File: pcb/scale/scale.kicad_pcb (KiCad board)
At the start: 2 copper layers, 103.8 x 47.9 mm, 89 parts, among them J1 USB_C_Receptacle_USB2.0, J2 Conn_01x07, J3 Conn_01x04, SW1 SW_Push, SW10 SW_Push, SW11 SW_Push, SW12 SW_Push, SW13 SW_Push, SW14 SW_Push, SW15 SW_Push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

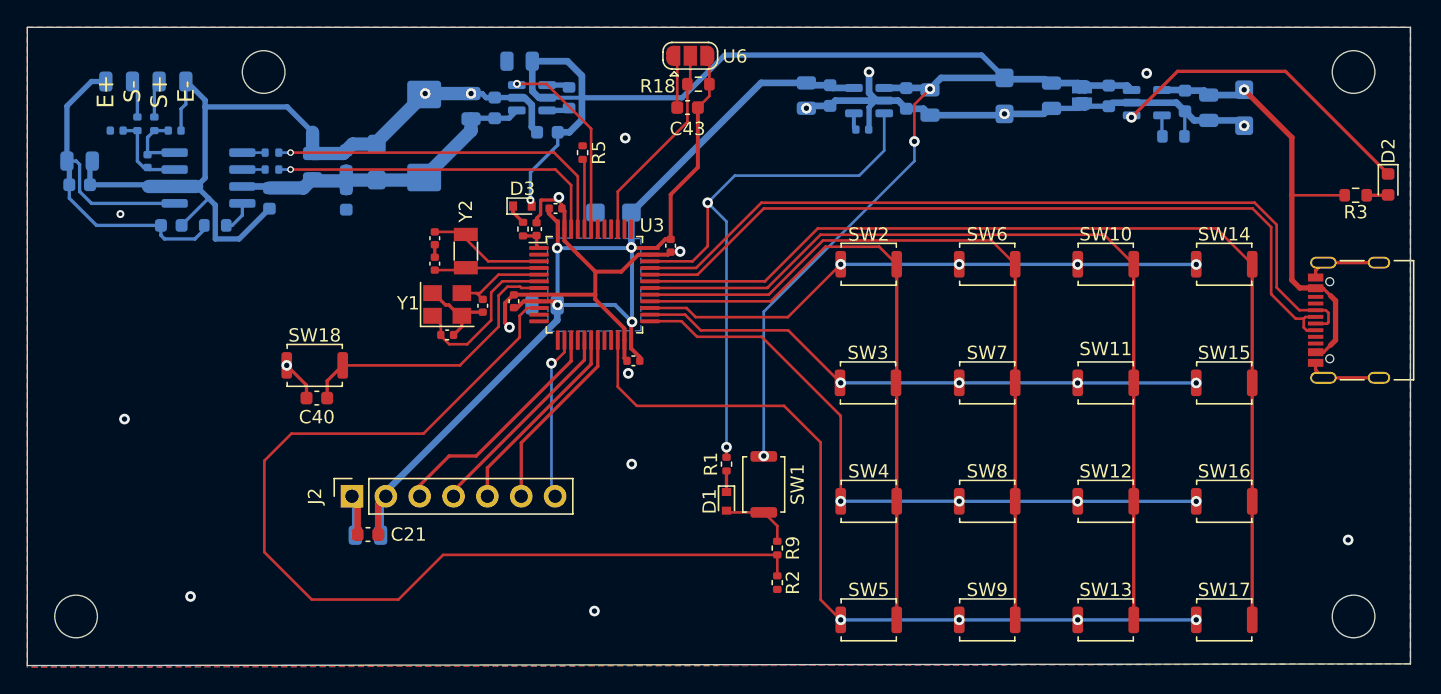
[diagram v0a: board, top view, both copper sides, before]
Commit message: 部分信号线加粗到0.25mm，电荷泵BATT+加粗到0.5mm
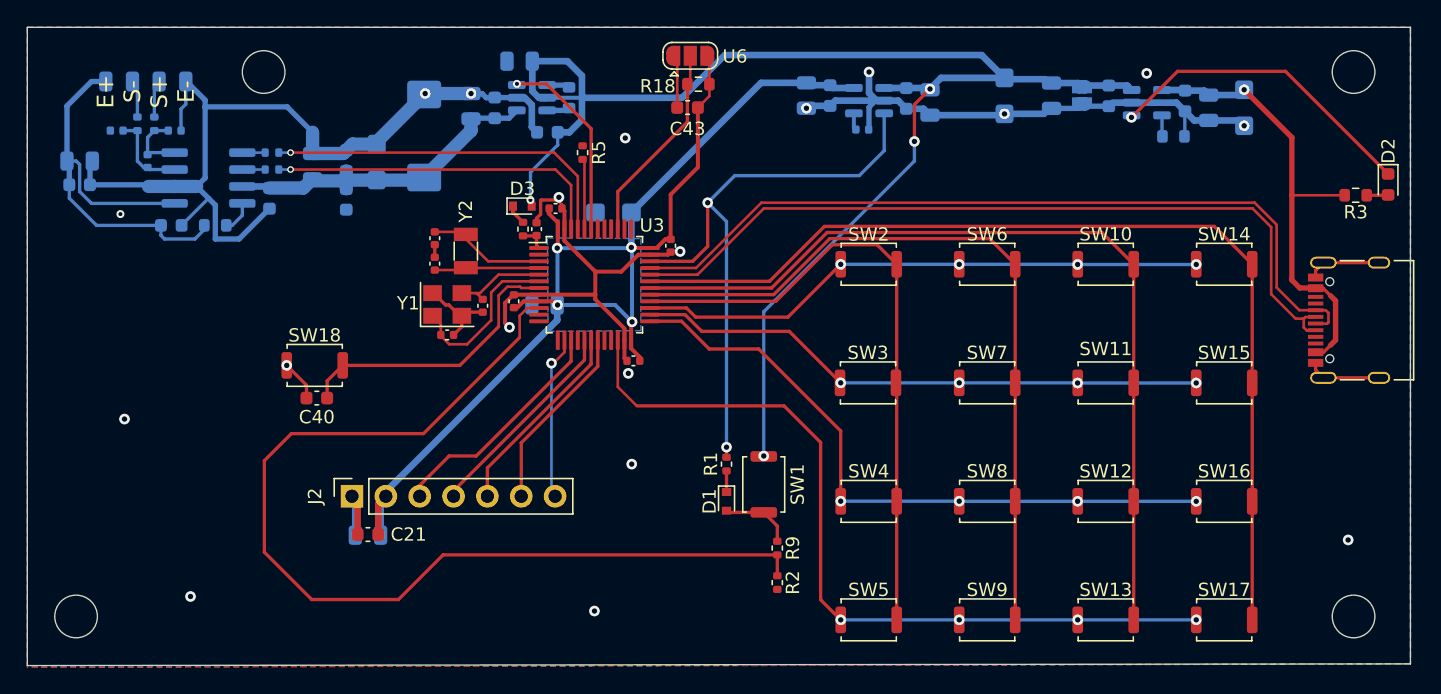
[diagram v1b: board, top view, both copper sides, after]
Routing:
- net /KB_Row3: track 50.3 -> 49.7 mm

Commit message: PCB添加文字
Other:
- board text added: "Copyright (c) 2022 Xu Ruijun License: GPL-3.0-or-later github.com/XuHg-zjcn/scale_hw"
- board text added: "桌面应变式电子秤 徐瑞骏 2022.11 v1.0 1687701765@qq.com"
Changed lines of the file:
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@@
   (gr_line (start 172.847 98.552) (end 69.088 98.679) (layer "Edge.Cuts") (width 0.1))
   (gr_line (start 69.088 98.679) (end 69.088 50.8) (layer "Edge.Cuts") (width 0.1))
+  (gr_text "桌面应变式电子秤\n徐瑞骏 2022.11 v1.0\n1687701765@qq.com" (at 143.59 72.92) (layer "B.SilkS")
+    (effects (font (size 1 1) (thickness 0.15)) (justify mirror))
+  )
+  (gr_text "Copyright (c) 2022  Xu Ruijun\nLicense: GPL-3.0-or-later\ngithub.com/XuHg-zjcn/scale_hw" (at 155.9 81.78) (layer "B.SilkS")
+    (effects (font (size 1 1) (thickness 0.15)) (justify left mirror))
+  )
   (gr_text "E+\nS-\nS+\nE-" (at 77.978 55.626 90) (layer "F.SilkS")
     (effects (font (size 1.25 1.25) (thickness 0.2)))

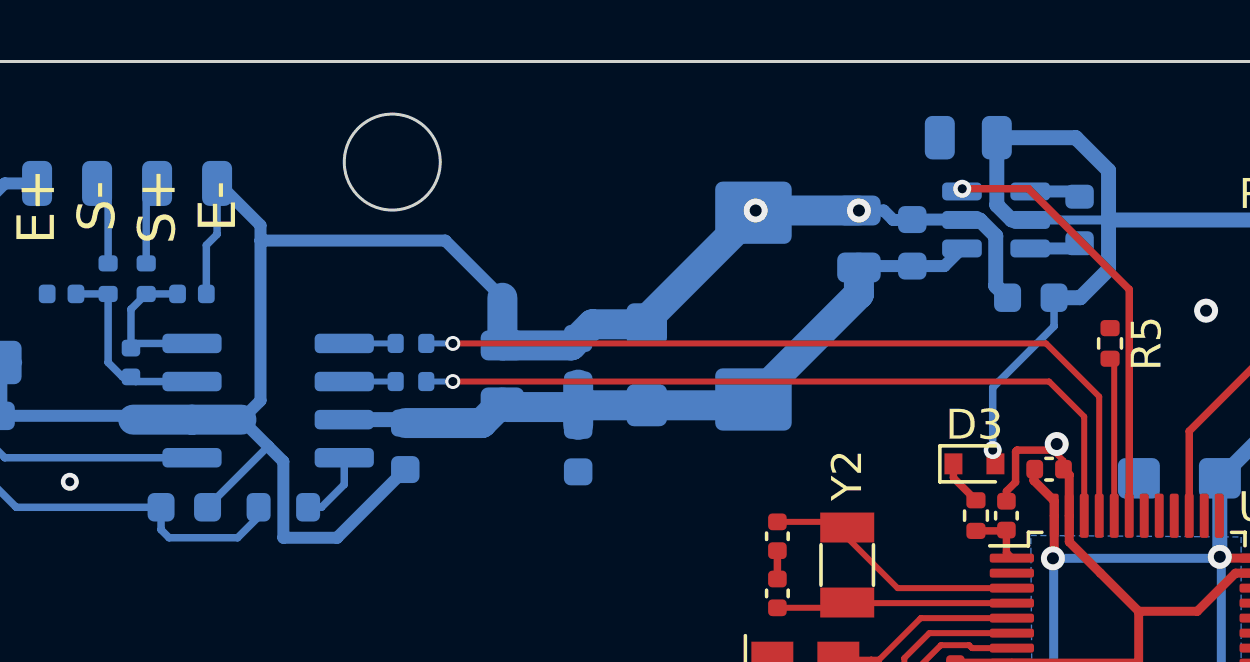
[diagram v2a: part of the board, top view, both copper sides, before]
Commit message: 添加接地过孔
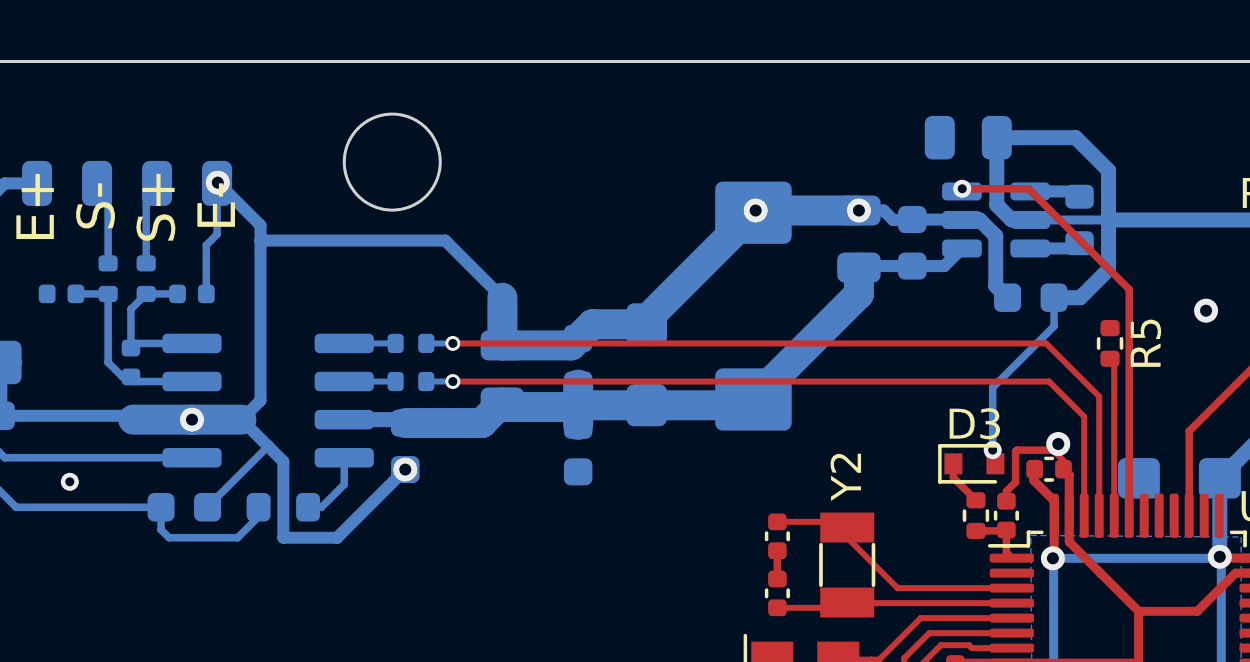
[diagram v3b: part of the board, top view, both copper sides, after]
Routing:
- net GND: vias 19 -> 22
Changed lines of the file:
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@@
   (segment (start 166.315 77.091) (end 170.485 77.091) (width 0.25) (layer "F.Cu") (net 2))
   (segment (start 165.735 75.971) (end 165.735 76.511) (width 0.25) (layer "F.Cu") (net 2))
-  (via (at 108.966 63.5508) (size 0.8) (drill 0.4) (layers "F.Cu" "B.Cu") (net 2))
+  (via (at 109.0168 63.5508) (size 0.8) (drill 0.4) (layers "F.Cu" "B.Cu") (net 2))
   (via (at 105.2576 73.3044) (size 0.8) (drill 0.4) (layers "F.Cu" "B.Cu") (net 2))
   (via (at 160.37115 58.1828) (size 0.8) (drill 0.4) (layers "F.Cu" "B.Cu") (net 2))
   (via (at 168.1734 89.2556) (size 0.8) (drill 0.4) (layers "F.Cu" "B.Cu") (free) (net 2))
   (via (at 88.547 76.16) (size 0.8) (drill 0.4) (layers "F.Cu" "B.Cu") (net 2))
+  (via (at 81.002 54.8372) (size 0.8) (drill 0.4) (layers "F.Cu" "B.Cu") (net 2))
   (via (at 142.3924 57.2938) (size 0.8) (drill 0.4) (layers "F.Cu" "B.Cu") (net 2))
+  (via (at 80.142 62.738) (size 0.8) (drill 0.4) (layers "F.Cu" "B.Cu") (net 2))
   (via (at 76.3778 80.1878) (size 0.8) (drill 0.4) (layers "F.Cu" "B.Cu") (free) (net 2))
   (via (at 81.3308 93.4974) (size 0.8) (drill 0.4) (layers "F.Cu" "B.Cu") (free) (net 2))
+  (via (at 87.2515 64.402) (size 0.8) (drill 0.4) (layers "F.Cu" "B.Cu") (net 2))
   (via (at 102.3733 55.7671) (size 0.8) (drill 0.4) (layers "F.Cu" "B.Cu") (net 2))
   (via (at 114.173 76.7588) (size 0.8) (drill 0.4) (layers "F.Cu" "B.Cu") (net 2))
@@
   (segment (start 148.3724 56.7188) (end 148.209 56.5554) (width 0.4) (layer "B.Cu") (net 2))
   (segment (start 80.6605 65.646) (end 82.6795 63.627) (width 0.25) (layer "B.Cu") (net 2))
+  (segment (start 81.002 54.8372) (end 80.978 54.8132) (width 0.4) (layer "B.Cu") (net 2))
   (segment (start 135.0264 56.909) (end 136.3246 56.909) (width 0.5) (layer "B.Cu") (net 2))
   (segment (start 132.2324 56.7944) (end 132.2324 58.4428) (width 0.4) (layer "B.Cu") (net 2))
@@
   (segment (start 129.7054 56.2988) (end 129.3114 56.6928) (width 0.5) (layer "B.Cu") (net 2))
   (segment (start 150.2209 56.7188) (end 148.3724 56.7188) (width 0.4) (layer "B.Cu") (net 2))
-  (segment (start 82.4255 56.2607) (end 80.978 54.8132) (width 0.4) (layer "B.Cu") (net 2))
+  (segment (start 82.4255 56.2607) (end 81.002 54.8372) (width 0.4) (layer "B.Cu") (net 2))
   (segment (start 80.6195 56.9215) (end 80.6195 58.547) (width 0.25) (layer "B.Cu") (net 2))
   (segment (start 151.9309 56.4518) (end 150.4879 56.4518) (width 0.5) (layer "B.Cu") (net 2))
